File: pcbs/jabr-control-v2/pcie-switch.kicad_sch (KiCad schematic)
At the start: 55 parts, among them U303 PI7C9X2G304SL

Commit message: PCI11010C Schematic sheet mostly done
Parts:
- removed C3001, C3002, C3005, C3006, C3007, C3008: 220n, project_footprints:C_0402, symbol DEV:C_TINY_IO
- removed C3003, C3004: 100n, project_footprints:C_0402, symbol DEV:C_SMALL_IO
- removed C303, C314, C331: 4u7, project_footprints:C_0402, symbol DEV:C_SMALL
- removed C304, C308, C309, C310, C311, C312, C313, C315, C316, C317, C318, C319, C320, C321, C322, C323, C324, C325, C326, C327, C328, C329, C330: 100n, project_footprints:C_0402, symbol DEV:C_SMALL
- removed R3001, R3002: 5k1, project_footprints:R_0402, symbol DEV:R_SMALL
- removed R313, R316, R317: 330R, symbol DEV:R_SMALL
- removed R314, R315: 5k1, symbol DEV:R_SMALL
- removed R318: 475R, project_footprints:R_0402, symbol DEV:R_SMALL
- removed R319: 1k43, project_footprints:R_0402, symbol DEV:R_SMALL
- removed TP303: 1.5mm, project_footprints:TestPoint_Pad_D1.5mm, symbol Connector:TestPoint_Small
- removed U303: PI7C9X2G304SL, project_footprints:QFP40P1600X1600X160-129N, symbol PCIE-FABRIC:PI7C9X2G304SL
- added C301, C302, C303, C304: 220n, project_footprints:C_0402, symbol DEV:C_TINY_IO
- added D301, D302: PMEG4002EL-QYL, project_footprints:PMEG4002EL-QYL, symbol DIODE:PMEG4002EL-QYL
- added Q301: DMN21D2UFB-7B, project_footprints:DMN21D2UFB7B, symbol MOSFET:DMN21D2UFB-7B
- added R301, R302, R304, R307, R308, R309: 10k, project_footprints:R_0402, symbol DEV:R_SMALL
- added R303: 1k5, project_footprints:R_0402, symbol DEV:R_SMALL
- added U301: SYA75603A, project_footprints:SYA7560x, symbol CLK-BUF:SYA75603A
- added U302: PCI11010C, project_footprints:PCI11010C, symbol PCIE-FABRIC:PCI11010C
- added Y301: XRCGB25M000F3A16R0, project_footprints:XRCGB25M000F3A16R0, symbol Device:Crystal_GND24_Small
- C305, C306: value 100n -> 10p
- C307: value 100n -> 1n
- R305: value 10k -> 200R
- R306: value 330R -> 10k
- R310: value 330R -> 100k; footprint (none) -> project_footprints:R_0402
- R311, R312: value 330R -> 10k; footprint (none) -> project_footprints:R_0402
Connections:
- net PWR_SAV is gone; now on net +3V3_PCIE: R306.1
- net TEST6 is gone; now on net +1V8: R311.1
- net +3V3_PCIE: now also R301.1, R304.1, R307.1, R308.1, U302.1 (VDD33), U302.100 (VSS), U302.14 (VDD33PA), U302.18 (VDD33PA), U302.23 (VDD33PVTREF), U302.27 (VDDVARIO), U302.33 (VDDVARIO), U302.35 (VDD33WRPLL), U302.51 (VDD33ENET), U302.69 (VDDVARIO), U302.74 (VDD33A1), U302.81 (VDD33PC), U302.86 (VDD33PC), U302.9 (VDD33PA), U302.96 (VDD33); no longer C305.1, C306.1, C307.1, R305.1
- net GND: now also C305.1, C306.1, R305.2, Q301.2 (S), R309.2, U301.17 (GND), U301.9 (GND), U302.100 (VSS), U302.24 (VSSPVTREF), U302.34 (VSSWRPLL), U302.65 (VSSXTAL), Y301.2 (G), Y301.4 (G); no longer C305.2, C306.2, R306.2, R311.2, R312.2
- net P0_TXN: now also C302.1, U302.11 (PCIE_TXM_L0_P0)
- net P0_TXP: now also C301.1, U302.10 (PCIE_TXP_L0_P0)
- net P1_TXN: now also C304.1, U302.83 (PCIE_TXM_L0_P1)
- net P1_TXP: now also C303.1, U302.82 (PCIE_TXP_L0_P1)
- net PORT0.CLK_N: now also U301.2 (IN_N)
- net PORT0.CLK_P: now also U301.1 (IN_P)
- net PORT0.RX_N: now also C302.2
- net PORT0.RX_P: now also C301.2
- net PORT0.TX_N: now also U302.7 (PCIE_RXM_L0_P0)
- net PORT0.TX_P: now also U302.6 (PCIE_RXP_L0_P0)
- net PORT1.CLK_N: now also U301.11 (OUT0_N)
- net PORT1.CLK_P: now also U301.10 (OUT0_P)
- net PORT1.RX_N: now also U302.79 (PCIE_RXM_L0_P1)
- net PORT1.RX_P: now also U302.78 (PCIE_RXP_L0_P1)
- net PORT1.TX_N: now also C304.2
- net PORT1.TX_P: now also C303.2
- net SMB.SCL: now also R304.2, U302.60 (PROG64/SCL_PU)
- net SMB.SDA: now also R307.2, U302.61 (PROG65/SDA_PU)
- net ~{RST}: now also C307.1, R306.2, D301.2 (A), U302.75 (~{RESET}); no longer R305.2
- net PORT1_STATUS: no longer names the net of TP302.1
- net PORT1_STATUS: now also R311.2, D302.2 (A), U301.12 (~{OE0})
- net PORT2_STATUS: no longer names the net of TP301.1
- net PORT2_STATUS: now also U301.16 (~{OE1})
- net TEST3 renamed +1V8
- net +1V8: now also R302.1, R303.1, U301.13 (VDD), U302.39 (VDDRGMII), U302.41 (PROG49), U302.55 (VDDRGMII)
- net TEST5 renamed TESTEN
- net TESTEN: now also U302.76 (TESTEN)
- new net: U301.3 (NC), U301.4 (NC), U301.5 (NC), U301.6 (NC), U301.7 (NC), U301.8 (NC)
- new net: R308.2, U302.64 (PROG68/SERIAL_SEL_STRAP)
- new net +1V1: U302.12 (VDD11PA), U302.13 (VDD11PA), U302.15 (VDD11PA), U302.19 (VDD11PA), U302.22 (VDD11), U302.38 (VDD11), U302.50 (VDD11ENET), U302.68 (VDD11XTAL), U302.73 (VDD11), U302.8 (VDD11PA), U302.80 (VDD11PC), U302.84 (VDD11PC), U302.85 (VDD11PC), U302.89 (VDD11)
- new net EEPROM_STRAP: R309.1, U302.94 (PROG79/EEPROM_STRAP)
- new net ENET_RESREF: R305.1, U302.52 (ENET_RESREF)
- new net LINK: Q301.3 (D), R312.2, U302.42 (PROG50)
- new net MDC: U302.36 (PROG46)
- new net MDIO: R303.2, U302.37 (PROG47)
- new net OSC_IN: C305.2, U302.66 (XTALI/CLK_IN), Y301.3
- new net OSC_OUT: C306.2, U302.67 (XTALO), Y301.1
- new net P0_CLK_N: U301.15 (OUT1_N), U302.88 (PCIE_REFCLK_IN_M)
- new net P0_CLK_P: U301.14 (OUT1_P), U302.87 (PCIE_REFCLK_IN_P)
- new net RX_CLK: U302.45 (PROG53)
- new net RX_CTL: U302.44 (PROG52)
- new net RX_D0: U302.46 (PROG54)
- new net RX_D1: U302.47 (PROG55)
- new net RX_D2: U302.48 (PROG56)
- new net RX_D3: U302.49 (PROG57)
- new net SMB_ALERT: U302.2 (PROG0)
- new net TX_CLK: U302.53 (PROG58)
- new net TX_CTL: U302.54 (PROG59)
- new net TX_D0: U302.56 (PROG60)
- new net TX_D1: U302.57 (PROG61)
- new net TX_D2: U302.58 (PROG62)
- new net TX_D3: U302.59 (PROG63)
- new net ~{LINK}: Q301.1 (G)
- new net ~{PCIE_CLKREQ}: U302.28 (PROG29)
- new net ~{PCIE_RST}: R301.2, U302.77 (~{PCIE_PERST})
- new net ~{PCIE_WAKE}: U302.29 (PROG30)
- new net ~{PHY_INT}: U302.43 (PROG51)
- new net ~{PHY_RST}: R302.2, U302.40 (PROG48)
- new net ~{PORT1_CLKREQ}: D302.1 (K)
- new net ~{RST_5V}: D301.1 (K)
- no-connect marks 23 -> 4
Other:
- note added: "Clock Buffer"
- note added: "From CM5"
- note added: "PCIe Switch & MAC"
- note added: "To M.2"
- note removed: "Input"
- note removed: "Output"
- note removed: "This is the clocking scheme of the switch. The buffering circuitry is separate from the PCIe circuitry, hence the need to connect REFCLKO_0 -> REFCLK."

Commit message: Moved M.2 buffers to new sheet
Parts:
- removed D302: PMEG4002EL-QYL, project_footprints:PMEG4002EL-QYL, symbol DIODE:PMEG4002EL-QYL
- removed R301: 10k, project_footprints:R_0402, symbol DEV:R_SMALL
- added R302: 10k, project_footprints:R_0402, symbol DEV:R_SMALL
- added TP303: 1.5mm, project_footprints:TestPoint_Pad_D1.5mm, symbol Connector:TestPoint_Small
- renumbered C307 to C305, C305 to C306, C306 to C307, R311 to R301, R309 to R303, R302 to R304, R303 to R305, R304 to R306, R312 to R308, R308 to R309, R305 to R311, R306 to R312, TP302 to TP301, TP301 to TP302
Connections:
- net +3V3_PCIE: now also R302.1
- net LINK: now also TP303.1
- net ~{PORT1_CLKREQ}: now also R301.2, TP301.1, U301.12 (~{OE0})
- net ~{OE1}: now reaches TP302.1, U301.16 (~{OE1})
- net SMB_ALERT renamed SMB.~{INT}
- net SMB.~{INT}: now also R302.2
- net ~{PCIE_CLKREQ} renamed ~{PORT0_CLKREQ}
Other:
- moved on the sheet: C301, C302, C303, C304, C305, C306, C307, D301, Q301, R301, R303, R304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

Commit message: Power circuitry done
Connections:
- net ~{RST} renamed ~{PCIE_PG}
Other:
- moved on the sheet: C305, D301
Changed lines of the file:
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@@
 	)
 	(junction
-		(at 360.68 134.62)
+		(at 208.28 91.44)
 		(diameter 0)
 		(color 0 0 0 0)
 	)
 	(junction
-		(at 208.28 91.44)
+		(at 375.92 162.56)
 		(diameter 0)
 		(color 0 0 0 0)
 	)
 	(junction
-		(at 375.92 162.56)
+		(at 297.18 116.84)
 		(diameter 0)
 		(color 0 0 0 0)
 	)
 	(junction
-		(at 297.18 116.84)
+		(at 370.84 134.62)
 		(diameter 0)
 		(color 0 0 0 0)
@@
 	)
 	(junction
+		(at 360.68 134.62)
+		(diameter 0)
+		(color 0 0 0 0)
+	)
+	(junction
 		(at 297.18 137.16)
 		(diameter 0)
@@
 	(wire
 		(pts
-			(xy 360.68 142.24) (xy 360.68 144.78)
+			(xy 360.68 144.78) (xy 360.68 147.32)
 		)
 		(stroke
@@
 	(wire
 		(pts
+			(xy 370.84 139.7) (xy 370.84 134.62)
+		)
+		(stroke
+			(width 0)
+			(type default)
+		)
+	)
+	(wire
+		(pts
 			(xy 297.18 175.26) (xy 297.18 177.8)
 		)
@@
 	(wire
 		(pts
+			(xy 381 139.7) (xy 370.84 139.7)
+		)
+		(stroke
+			(width 0)
+			(type default)
+		)
+	)
+	(wire
+		(pts
 			(xy 347.98 101.6) (xy 347.98 104.14)
 		)
@@
 	(wire
 		(pts
-			(xy 375.92 134.62) (xy 378.46 134.62)
+			(xy 378.46 134.62) (xy 381 134.62)
 		)
 		(stroke
@@
 	(wire
 		(pts
-			(xy 360.68 134.62) (xy 360.68 137.16)
+			(xy 360.68 134.62) (xy 360.68 139.7)
 		)
 		(stroke
@@
 		)
 	)
+	(wire
+		(pts
+			(xy 370.84 134.62) (xy 373.38 134.62)
+		)
+		(stroke
+			(width 0)
+			(type default)
+		)
+	)
 	(polyline
 		(pts
@@
 	(hierarchical_label "~{RST_5V}"
 		(shape input)
-		(at 378.46 134.62 0)
+		(at 381 134.62 0)
+		(effects
+			(font
+				(size 1.27 1.27)
+			)
+			(justify left)
+		)
+	)
+	(hierarchical_label "~{PCIE_PG}"
+		(shape input)
+		(at 381 139.7 0)
 		(effects
 			(font
@@
 	(symbol
 		(lib_id "DEV:C_SMALL")
-		(at 360.68 139.7 0)
+		(at 360.68 142.24 0)
 		(unit 1)
 		(body_style 1)
@@
 		(dnp no)
 		(property "Reference" "C305"
-			(at 363.22 138.4362 0)
+			(at 363.22 140.9762 0)
 			(show_name no)
 			(do_not_autoplace no)
@@
 		)
 		(property "Value" "1n"
-			(at 363.22 140.9762 0)
+			(at 363.22 143.5162 0)
 			(show_name no)
 			(do_not_autoplace no)
@@
 		)
 		(property "Footprint" "project_footprints:C_0402"
-			(at 360.68 139.7 0)
+			(at 360.68 142.24 0)
 			(hide yes)
 			(show_name no)
@@
 		)
 		(property "Datasheet" ""
-			(at 360.68 139.7 0)
+			(at 360.68 142.24 0)
 			(hide yes)
 			(show_name no)
@@
 		)
 		(property "Description" "Unpolarized capacitor, small symbol"
-			(at 360.68 139.7 0)
+			(at 360.68 142.24 0)
 			(hide yes)
 			(show_name no)
@@
 		)
 		(property "Field6" ""
-			(at 360.68 139.7 0)
+			(at 360.68 142.24 0)
 			(hide yes)
 			(show_name no)
@@
 		)
 		(property "Field7" ""
-			(at 360.68 139.7 0)
+			(at 360.68 142.24 0)
 			(hide yes)
 			(show_name no)
@@
 		)
 		(property "Part Description" ""
-			(at 360.68 139.7 0)
+			(at 360.68 142.24 0)
 			(hide yes)
 			(show_name no)
@@
 	(symbol
 		(lib_id "power:GND")
-		(at 360.68 144.78 0)
+		(at 360.68 147.32 0)
 		(unit 1)
 		(body_style 1)
@@
 		(fields_autoplaced yes)
 		(property "Reference" "#PWR0315"
-			(at 360.68 151.13 0)
+			(at 360.68 153.67 0)
 			(hide yes)
 			(show_name no)
@@
 		)
 		(property "Value" "GND"
-			(at 360.68 149.86 0)
+			(at 360.68 152.4 0)
 			(show_name no)
 			(do_not_autoplace no)
@@
 		)
 		(property "Footprint" ""
-			(at 360.68 144.78 0)
+			(at 360.68 147.32 0)
 			(hide yes)
 			(show_name no)
@@
 		)
 		(property "Datasheet" ""
-			(at 360.68 144.78 0)
+			(at 360.68 147.32 0)
 			(hide yes)
 			(show_name no)
@@
 		)
 		(property "Description" "Power symbol creates a global label with name \"GND\" , ground"
-			(at 360.68 144.78 0)
+			(at 360.68 147.32 0)
 			(hide yes)
 			(show_name no)
@@
 	(symbol
 		(lib_id "DIODE:PMEG4002EL-QYL")
-		(at 373.38 134.62 0)
+		(at 375.92 134.62 0)
 		(mirror y)
 		(unit 1)
@@
 		(dnp no)
 		(property "Reference" "D301"
-			(at 373.38 132.08 0)
+			(at 375.92 132.08 0)
 			(show_name no)
 			(do_not_autoplace no)
@@
 		)
 		(property "Value" "PMEG4002EL-QYL"
-			(at 373.38 129.54 0)
+			(at 375.92 129.54 0)
 			(show_name no)
 			(do_not_autoplace no)
@@
 		)
 		(property "Footprint" "project_footprints:PMEG4002EL-QYL"
-			(at 373.38 134.62 0)
+			(at 375.92 134.62 0)
 			(hide yes)
 			(show_name no)
@@
 		)
 		(property "Datasheet" "https://assets.nexperia.com/documents/data-sheet/PMEG4002EL-Q.pdf"
-			(at 373.38 134.62 90)
+			(at 375.92 134.62 90)
 			(hide yes)
 			(show_name no)
@@
 		)
 		(property "Description" "Diode, small symbol"
-			(at 373.38 134.62 0)
+			(at 375.92 134.62 0)
 			(hide yes)
 			(show_name no)
@@
 		)
 		(property "Sim.Device" "D"
-			(at 373.38 134.62 0)
+			(at 375.92 134.62 0)
 			(hide yes)
 			(show_name no)
@@
 		)
 		(property "Sim.Pins" "1=K 2=A"
-			(at 373.38 134.62 0)
+			(at 375.92 134.62 0)
 			(hide yes)
 			(show_name no)
@@
 		)
 		(property "Field6" ""
-			(at 373.38 134.62 0)
+			(at 375.92 134.62 0)
 			(hide yes)
 			(show_name no)
@@
 		)
 		(property "Field7" ""
-			(at 373.38 134.62 0)
+			(at 375.92 134.62 0)
 			(hide yes)
 			(show_name no)
@@
 		)
 		(property "Part Description" ""
-			(at 373.38 134.62 0)
+			(at 375.92 134.62 0)
 			(hide yes)
 			(show_name no)

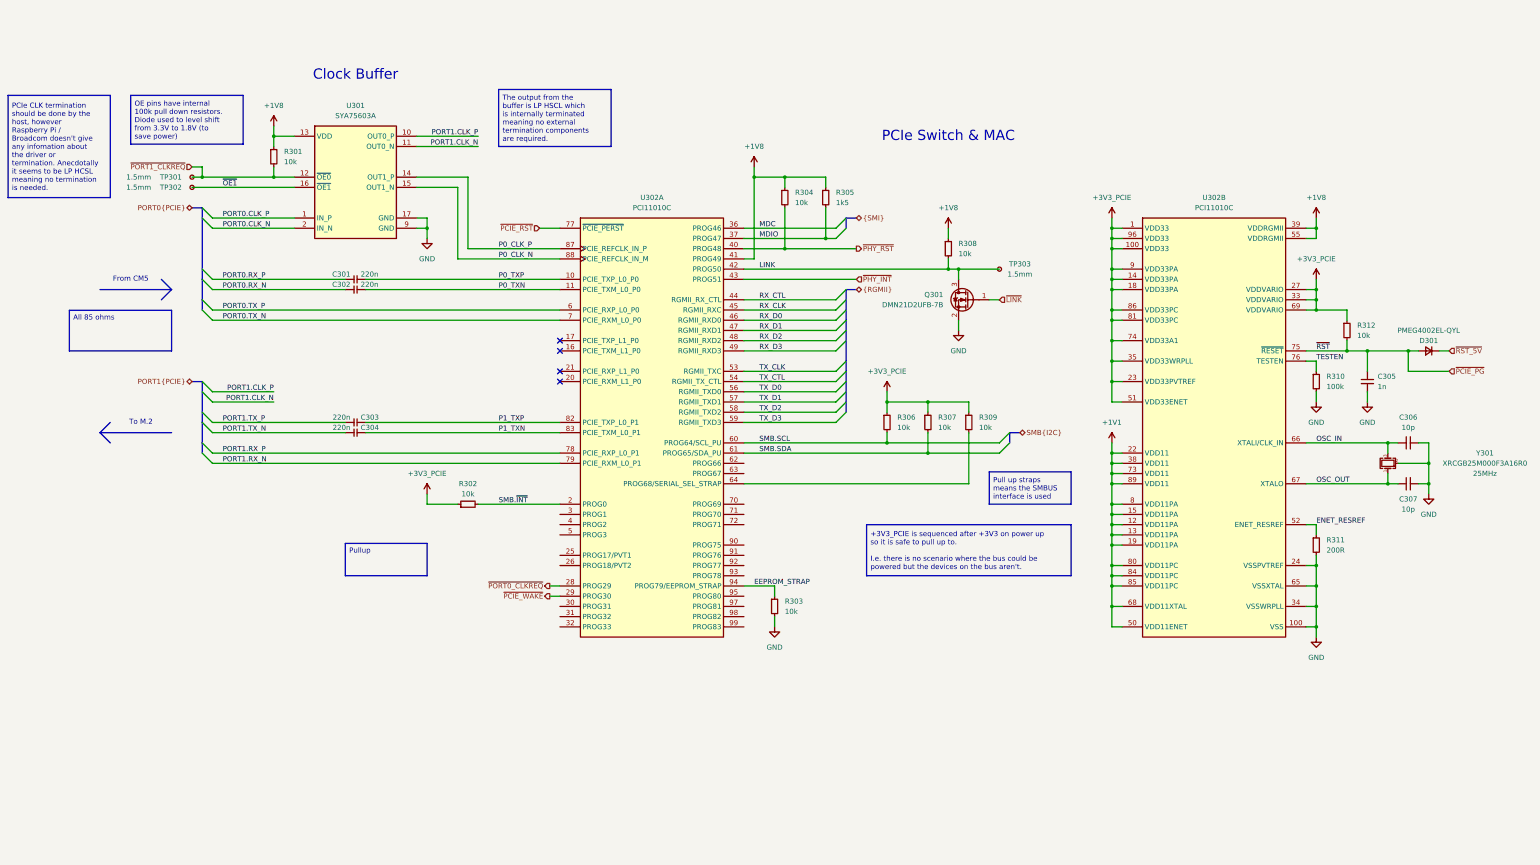
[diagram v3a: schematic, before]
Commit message: PCI11010 IO done
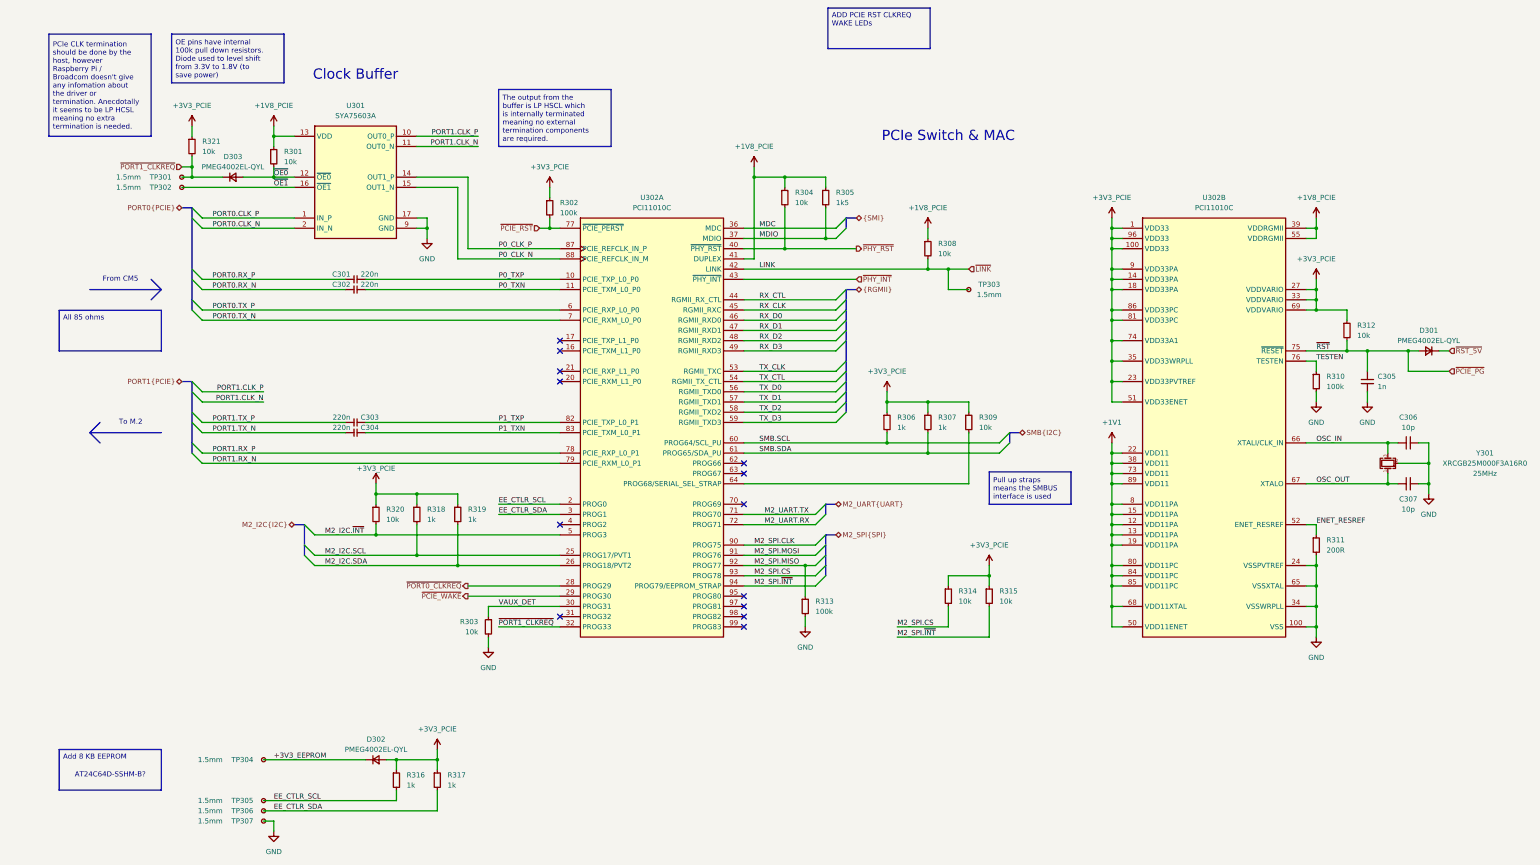
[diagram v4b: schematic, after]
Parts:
- removed Q301: DMN21D2UFB-7B, project_footprints:DMN21D2UFB7B, symbol MOSFET:DMN21D2UFB-7B
- added D302, D303: PMEG4002EL-QYL, project_footprints:PMEG4002EL-QYL, symbol DIODE:PMEG4002EL-QYL
- added R313: 100k, project_footprints:R_0402, symbol DEV:R_SMALL
- added R314, R315, R320, R321: 10k, project_footprints:R_0402, symbol DEV:R_SMALL
- added R316, R317, R318, R319: 1k, project_footprints:R_0402, symbol DEV:R_SMALL
- added TP304, TP305, TP306, TP307: 1.5mm, project_footprints:TestPoint_Pad_D1.5mm, symbol Connector:TestPoint_Small
- R302: value 10k -> 100k
- R306, R307: value 10k -> 1k
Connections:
- net LINK is gone; now on net ~{LINK}: R308.2, TP303.1, U302.42 (PROG50)
- net +3V3_PCIE: now also D302.2 (A), R314.1, R315.1, R316.1, R317.1, R318.1, R319.1, R320.1, R321.1
- net GND: now also R313.2, TP307.1
- net ~{PCIE_RST}: now also R302.2
- net ~{PORT1_CLKREQ}: now also U302.32 (PROG33), D303.1 (K), R321.2; no longer R301.2, U301.12 (~{OE0})
- net M2_I2C.SCL: now reaches U302.25 (PROG17/PVT1)
- net M2_I2C.SCL: now also R318.2
- net M2_I2C.SDA: now reaches U302.26 (PROG18/PVT2)
- net M2_I2C.SDA: now also R319.2
- net EE_CTLR_SDA: now reaches U302.3 (PROG1)
- net EE_CTLR_SDA: now also R317.2, TP306.1
- net VAUX_DET: now reaches U302.30 (PROG31)
- net VAUX_DET: now also R303.1
- net M2_I2C.~{INT}: now reaches U302.5 (PROG3)
- net M2_I2C.~{INT}: now also R320.2
- net M2_UART.TX: now reaches U302.71 (PROG70)
- net M2_UART.RX: now reaches U302.72 (PROG71)
- net M2_SPI.CLK: now reaches U302.90 (PROG75)
- net M2_SPI.MOSI: now reaches U302.91 (PROG76)
- net M2_SPI.MISO: now reaches U302.92 (PROG77)
- net M2_SPI.MISO: now also R313.1
- net M2_SPI.CS: now reaches U302.93 (PROG78)
- net M2_SPI.CS: now also R314.2
- net +1V8 renamed +1V8_PCIE
- net EEPROM_STRAP renamed M2_SPI.~{INT}
- net M2_SPI.~{INT}: now also R315.2; no longer R303.1
- net SMB.~{INT} renamed EE_CTLR_SCL
- net EE_CTLR_SCL: now also R316.2, TP305.1; no longer R302.2
- new net +3V3_EEPROM: D302.1 (K), TP304.1
- new net ~{OE0}: D303.2 (A), R301.2, U301.12 (~{OE0})
- no-connect marks 4 -> 13
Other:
- note added: "AT24C64D-SSHM-B?"
- moved on the sheet: R308, TP301, TP302, TP303
